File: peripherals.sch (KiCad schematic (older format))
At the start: 29 parts, among them J3 RS232, Q1 NMOS ??, Q2 PZT2222A*, U2 25LCxxx, U5 Mystery comp, U6 MAX3226*

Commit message: Add missing components, mostly around Mystery U5 IC.
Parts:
- added C19, C25, C55: C, symbol Device:C_Small
- added R13: R*, symbol Device:R_Small
- added R6: 4.7k*, symbol Device:R_Small
- added R7: 4.7k, symbol Device:R_Small
- added TP14: CS_Flash, symbol Connector:TestPoint
- added TP15: SCL, symbol Connector:TestPoint
- added TP16: SDA, symbol Connector:TestPoint
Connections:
- net labels added: U5_INT
- net labels removed: U5_CS
- wire segments 89 -> 115

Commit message: Fill in more missing components
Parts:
- removed R21, R28: 0, symbol Device:R_Small
- added C15: C, symbol Device:C_Small
- added C3: C, symbol Device:C
- added R21, R28: Jumper_2_Bridged, symbol Jumper:Jumper_2_Bridged
- C30: value C* -> C
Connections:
- wire segments 115 -> 120
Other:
- note added: "Despite missing R6, SDA is still pulled to\n+3.3V through R41 (COL1) by about 30k Ohm."
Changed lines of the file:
@@
 Sheet 3 3
 Title "SMART Response XE - Peripherals"
-Date "2021-09-08"
+Date "2021-09-09"
 Rev ""
 Comp ""
@@
 $EndComp
 Wire Wire Line
-	1550 2950 2150 2950
+	1650 2950 2150 2950
 Wire Wire Line
 	2150 3650 2050 3650
@@
 AR Path="/61400672/6143FF32" Ref="C30"  Part="1"
 F 0 "C30" H 1815 1846 50  0000 L CNN
-F 1 "C*" H 1815 1755 50  0000 L CNN
+F 1 "C" H 1815 1755 50  0000 L CNN
 F 2 "" H 1738 1650 50  0001 C CNN
 F 3 "~" H 1700 1800 50  0001 C CNN
@@
 $Comp
 L Device:R_Small R?
-U 1 1 614D1534
-P 1450 3200
-AR Path="/614D1534" Ref="R?"  Part="1"
-AR Path="/61400672/614D1534" Ref="R21"  Part="1"
-F 0 "R21" V 1350 3100 50  0000 L CNN
-F 1 "0" V 1350 3300 50  0000 L CNN
-F 2 "" H 1450 3200 50  0001 C CNN
-F 3 "~" H 1450 3200 50  0001 C CNN
-	1    1450 3200
-	0    1    1    0
-$EndComp
-$Comp
-L Device:R_Small R?
-U 1 1 614D153A
-P 1450 2950
-AR Path="/614D153A" Ref="R?"  Part="1"
-AR Path="/61400672/614D153A" Ref="R28"  Part="1"
-F 0 "R28" V 1550 2850 50  0000 L CNN
-F 1 "0" V 1550 3050 50  0000 L CNN
-F 2 "" H 1450 2950 50  0001 C CNN
-F 3 "~" H 1450 2950 50  0001 C CNN
-	1    1450 2950
-	0    1    -1   0
-$EndComp
-Text HLabel 1250 3200 0    50   Input ~ 0
-RX
-Text HLabel 1250 2950 0    50   Input ~ 0
-TX
-$Comp
-L Device:R_Small R?
 U 1 1 6143FF48
 P 1850 3650
@@
 L power:GND #PWR?
 U 1 1 61A6B179
-P 5950 6650
+P 5950 6950
 AR Path="/61A6B179" Ref="#PWR?"  Part="1"
 AR Path="/61400672/61A6B179" Ref="#PWR0135"  Part="1"
-F 0 "#PWR0135" H 5950 6400 50  0001 C CNN
-F 1 "GND" H 5800 6600 50  0001 C CNN
-F 2 "" H 5950 6650 50  0001 C CNN
-F 3 "" H 5950 6650 50  0001 C CNN
-	1    5950 6650
+F 0 "#PWR0135" H 5950 6700 50  0001 C CNN
+F 1 "GND" H 5800 6900 50  0001 C CNN
+F 2 "" H 5950 6950 50  0001 C CNN
+F 3 "" H 5950 6950 50  0001 C CNN
+	1    5950 6950
 	1    0    0    -1
 $EndComp
@@
 	1600 3650 1600 3600
 Wire Wire Line
-	1350 3200 1250 3200
-Wire Wire Line
-	1250 2950 1350 2950
-Wire Wire Line
-	1550 3200 2050 3200
+	1650 3200 2050 3200
 Wire Wire Line
 	2050 3200 2050 3350
@@
 	1    0    0    -1
 $EndComp
+$Comp
+L Jumper:Jumper_2_Bridged R28
+U 1 1 642D53D1
+P 1450 2950
+F 0 "R28" H 1450 3053 50  0000 C CNN
+F 1 "Jumper_2_Bridged" H 1450 3054 50  0001 C CNN
+F 2 "" H 1450 2950 50  0001 C CNN
+F 3 "~" H 1450 2950 50  0001 C CNN
+	1    1450 2950
+	1    0    0    -1
+$EndComp
+$Comp
+L Jumper:Jumper_2_Bridged R21
+U 1 1 642D5E0D
+P 1450 3200
+F 0 "R21" H 1450 3303 50  0000 C CNN
+F 1 "Jumper_2_Bridged" H 1450 3304 50  0001 C CNN
+F 2 "" H 1450 3200 50  0001 C CNN
+F 3 "~" H 1450 3200 50  0001 C CNN
+	1    1450 3200
+	1    0    0    -1
+$EndComp
+Wire Wire Line
+	1150 2950 1250 2950
+Wire Wire Line
+	1250 3200 1150 3200
+Text HLabel 1150 2950 0    50   Input ~ 0
+TX
+Text HLabel 1150 3200 0    50   Input ~ 0
+RX
+$Comp
+L Device:C C3
+U 1 1 642EE53F
+P 4700 1800
+F 0 "C3" H 4815 1846 50  0000 L CNN
+F 1 "C" H 4815 1755 50  0000 L CNN
+F 2 "" H 4738 1650 50  0001 C CNN
+F 3 "~" H 4700 1800 50  0001 C CNN
+	1    4700 1800
+	1    0    0    -1
+$EndComp
+$Comp
+L power:GND #PWR04
+U 1 1 642EF942
+P 4700 1950
+F 0 "#PWR04" H 4700 1700 50  0001 C CNN
+F 1 "GND" H 4705 1777 50  0000 C CNN
+F 2 "" H 4700 1950 50  0001 C CNN
+F 3 "" H 4700 1950 50  0001 C CNN
+	1    4700 1950
+	1    0    0    -1
+$EndComp
+$Comp
+L power:+3.3V #PWR03
+U 1 1 642EFF1C
+P 4700 1650
+F 0 "#PWR03" H 4700 1500 50  0001 C CNN
+F 1 "+3.3V" H 4715 1823 50  0000 C CNN
+F 2 "" H 4700 1650 50  0001 C CNN
+F 3 "" H 4700 1650 50  0001 C CNN
+	1    4700 1650
+	1    0    0    -1
+$EndComp
+$Comp
+L power:+3.3V #PWR05
+U 1 1 642FD893
+P 6350 6850
+F 0 "#PWR05" H 6350 6700 50  0001 C CNN
+F 1 "+3.3V" H 6365 7023 50  0000 C CNN
+F 2 "" H 6350 6850 50  0001 C CNN
+F 3 "" H 6350 6850 50  0001 C CNN
+	1    6350 6850
+	1    0    0    -1
+$EndComp
+$Comp
+L Device:C_Small C15
+U 1 1 642FBEA6
+P 6150 6900
+F 0 "C15" V 5921 6900 50  0000 C CNN
+F 1 "C" V 6012 6900 50  0000 C CNN
+F 2 "" H 6150 6900 50  0001 C CNN
+F 3 "~" H 6150 6900 50  0001 C CNN
+	1    6150 6900
+	0    1    1    0
+$EndComp
+Wire Wire Line
+	5950 6650 5950 6900
+Wire Wire Line
+	5950 6900 6050 6900
+Connection ~ 5950 6900
+Wire Wire Line
+	5950 6900 5950 6950
+Wire Wire Line
+	6250 6900 6350 6900
+Wire Wire Line
+	6350 6900 6350 6850
+Text Notes 8400 6150 0    50   ~ 0
+Despite missing R6, SDA is still pulled to\n+3.3V through R41 (COL1) by about 30k Ohm.
 $EndSCHEMATC

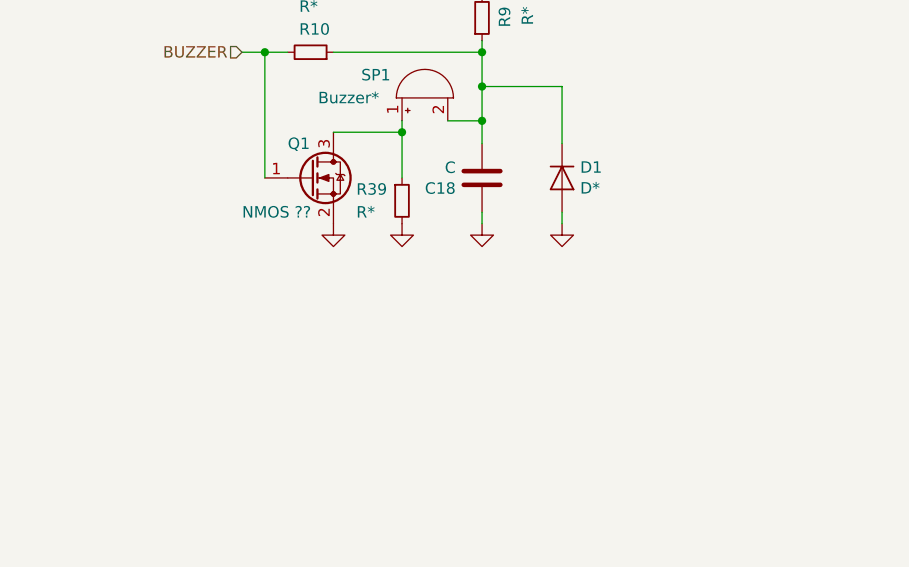
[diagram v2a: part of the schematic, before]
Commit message: Added comment concerning Q1 pinout on peripherals.sch
peripherals.sch, README.md:
	added a comment explaining that Q1 drain and source are swapped on
the main board.

Updated pdf of schematic
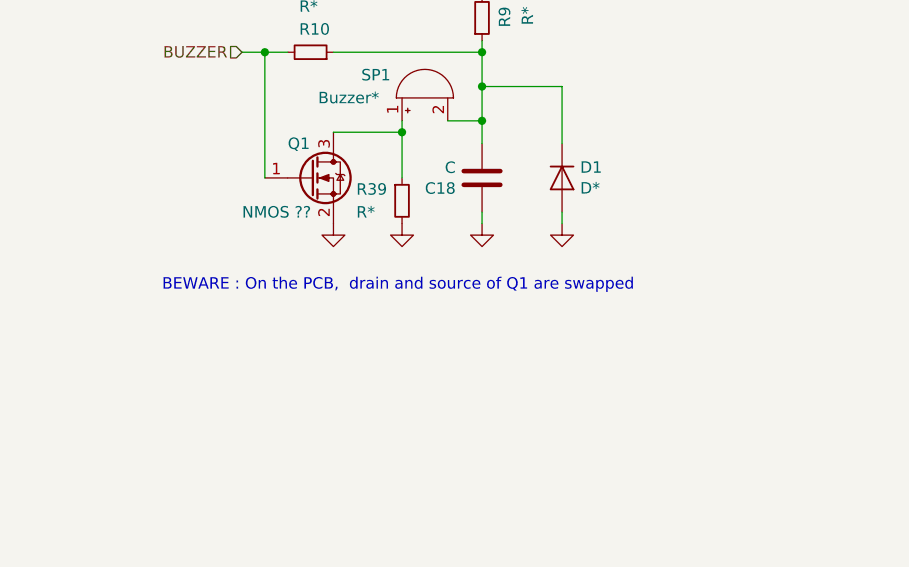
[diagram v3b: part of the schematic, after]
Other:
- note added: "BEWARE : On the PCB, drain and source of Q1 are swapped"
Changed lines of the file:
@@
 Text Notes 8400 6150 0    50   ~ 0
 Despite missing R6, SDA is still pulled to\n+3.3V through R41 (COL1) by about 30k Ohm.
+Text Notes 7950 2950 0    50   ~ 0
+BEWARE : On the PCB,  drain and source of Q1 are swapped
 $EndSCHEMATC
